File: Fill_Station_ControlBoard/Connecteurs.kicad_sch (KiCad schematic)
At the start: 45 parts, among them J3 USB_C_Receptacle_USB2.0_14P, J4 DE9_Pins, J6 RJ45_Wuerth_7499010211A, U2 USBLC6-2SC6, U3 MCP2561-E-P, U5 LAN8742A

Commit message: petites modifs pour ethernet + usb
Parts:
- added C35: 10n, symbol Device:C
- C11: value ~ -> 10n
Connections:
- net GND: now also C35.2; no longer J3.S1 (SHIELD)
- new net: C35.1, J3.S1 (SHIELD)
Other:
- note added: "Placer esd très proche du port"
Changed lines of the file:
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@@
 		)
 	)
+	(text "Placer esd très proche du port\n"
+		(exclude_from_sim no)
+		(at 316.484 36.322 0)
+		(effects
+			(font
+				(size 1.27 1.27)
+			)
+		)
+	)
 	(text "C'est normal que la pin VDDCR n'est pas alimenté - mettre les cap très proche de la chip\n"
 		(exclude_from_sim no)
@@
 	)
 	(junction
-		(at 294.64 101.6)
-		(diameter 0)
-		(color 0 0 0 0)
-	)
-	(junction
 		(at 88.9 189.23)
 		(diameter 0)
@@
 	)
 	(junction
+		(at 294.64 106.68)
+		(diameter 0)
+		(color 0 0 0 0)
+	)
+	(junction
 		(at 49.53 72.39)
 		(diameter 0)
@@
 	(wire
 		(pts
-			(xy 287.02 101.6) (xy 294.64 101.6)
-		)
-		(stroke
-			(width 0)
-			(type default)
-		)
-	)
-	(wire
-		(pts
 			(xy 152.4 64.77) (xy 119.38 64.77)
 		)
@@
 	(wire
 		(pts
-			(xy 294.64 99.06) (xy 294.64 101.6)
+			(xy 294.64 99.06) (xy 294.64 106.68)
+		)
+		(stroke
+			(width 0)
+			(type default)
+		)
+	)
+	(wire
+		(pts
+			(xy 294.64 106.68) (xy 294.64 109.22)
 		)
 		(stroke
@@
 	(wire
 		(pts
+			(xy 287.02 106.68) (xy 294.64 106.68)
+		)
+		(stroke
+			(width 0)
+			(type default)
+		)
+	)
+	(wire
+		(pts
 			(xy 93.98 199.39) (xy 93.98 217.17)
 		)
@@
 	(wire
 		(pts
-			(xy 294.64 101.6) (xy 294.64 104.14)
-		)
-		(stroke
-			(width 0)
-			(type default)
-		)
-	)
-	(wire
-		(pts
 			(xy 314.96 78.74) (xy 314.96 81.28)
 		)
@@
 		)
 	)
-	(wire
-		(pts
-			(xy 287.02 99.06) (xy 287.02 101.6)
-		)
-		(stroke
-			(width 0)
-			(type default)
-		)
-	)
 	(label "LED2"
 		(at 149.86 232.41 0)
@@
 	(symbol
 		(lib_id "power:GND")
-		(at 294.64 104.14 0)
+		(at 294.64 109.22 0)
 		(unit 1)
 		(exclude_from_sim no)
@@
 		(fields_autoplaced yes)
 		(property "Reference" "#PWR014"
-			(at 294.64 110.49 0)
+			(at 294.64 115.57 0)
 			(effects
 				(font
@@
 		)
 		(property "Value" "GND"
-			(at 294.64 109.22 0)
+			(at 294.64 114.3 0)
 			(effects
 				(font
@@
 		)
 		(property "Footprint" ""
-			(at 294.64 104.14 0)
+			(at 294.64 109.22 0)
 			(effects
 				(font
@@
 		)
 		(property "Datasheet" ""
-			(at 294.64 104.14 0)
+			(at 294.64 109.22 0)
 			(effects
 				(font
@@
 		)
 		(property "Description" "Power symbol creates a global label with name \"GND\" , ground"
-			(at 294.64 104.14 0)
+			(at 294.64 109.22 0)
 			(effects
 				(font
@@
 			)
 		)
-		(property "Value" "~"
+		(property "Value" "10n"
 			(at 240.03 231.1399 0)
 			(effects
@@
 					(unit 1)
 				)
+			)
+		)
+	)
+	(symbol
+		(lib_id "Device:C")
+		(at 287.02 102.87 0)
+		(unit 1)
+		(exclude_from_sim no)
+		(in_bom yes)
+		(on_board yes)
+		(dnp no)
+		(property "Reference" "C35"
+			(at 290.83 101.5999 0)
+			(effects
+				(font
+					(size 1.27 1.27)
+				)
+				(justify left)
+			)
+		)
+		(property "Value" "10n"
+			(at 290.83 104.1399 0)
+			(effects
+				(font
+					(size 1.27 1.27)
+				)
+				(justify left)
+			)
+		)
+		(property "Footprint" ""
+			(at 287.9852 106.68 0)
+			(effects
+				(font
+					(size 1.27 1.27)
+				)
+				(hide yes)
+			)
+		)
+		(property "Datasheet" "~"
+			(at 287.02 102.87 0)
+			(effects
+				(font
+					(size 1.27 1.27)
+				)
+				(hide yes)
+			)
+		)
+		(property "Description" "Unpolarized capacitor"
+			(at 287.02 102.87 0)
+			(effects
+				(font
+					(size 1.27 1.27)
+				)
+				(hide yes)
+			)
+		)
+		(pin "1"
+		)
+		(pin "2"
+		)
+		(instances
+			(project "Fill_Station_ControlBoard"
+				(path "/eaacffe0-ee57-428e-a37e-5655e0922ccc/08c8ede8-1095-4e69-9f52-7f615080da19"
+					(reference "C35")
+					(unit 1)
+				)

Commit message: heater
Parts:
- removed D4: D, symbol Device:D
- added R41: 100, symbol Device:R_US
- added U4: TCAN337G, symbol Interface_CAN_LIN:TCAN337G
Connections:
- net +3.3V is gone; now on net 3V3: R6.1
- net +5V: now also D3.1 (K), F3.2
- net TX_N: now reaches J6.2 (TD-), U5.20 (TXN)
- net TX_N: now also R41.2
- net TX_P: now reaches J6.1 (TD+), U5.21 (TXP)
- net TX_P: now also R41.1
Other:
- note added: "pull up?"

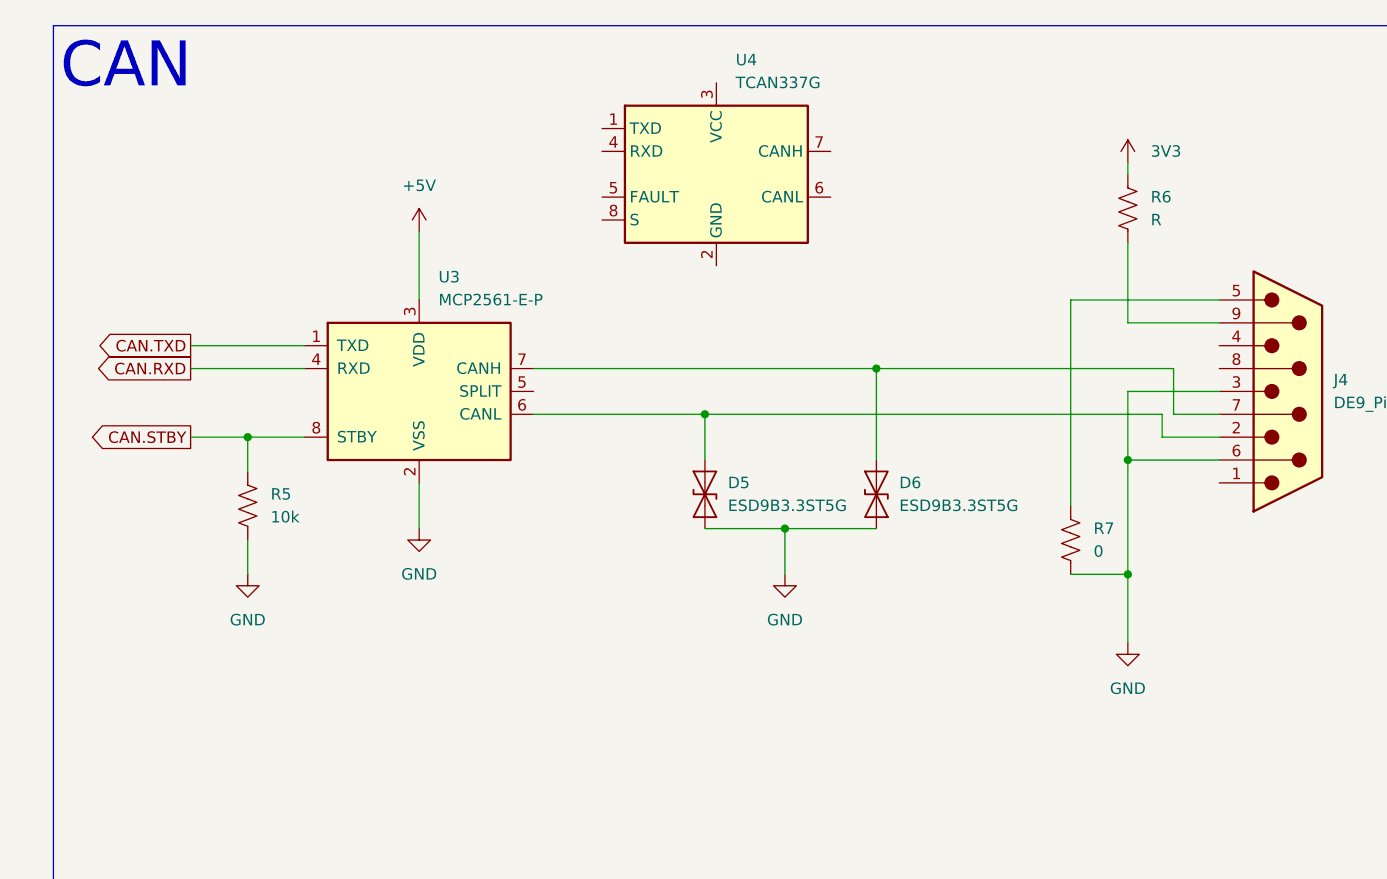
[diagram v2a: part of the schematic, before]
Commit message: Développer plus le circuit CAN
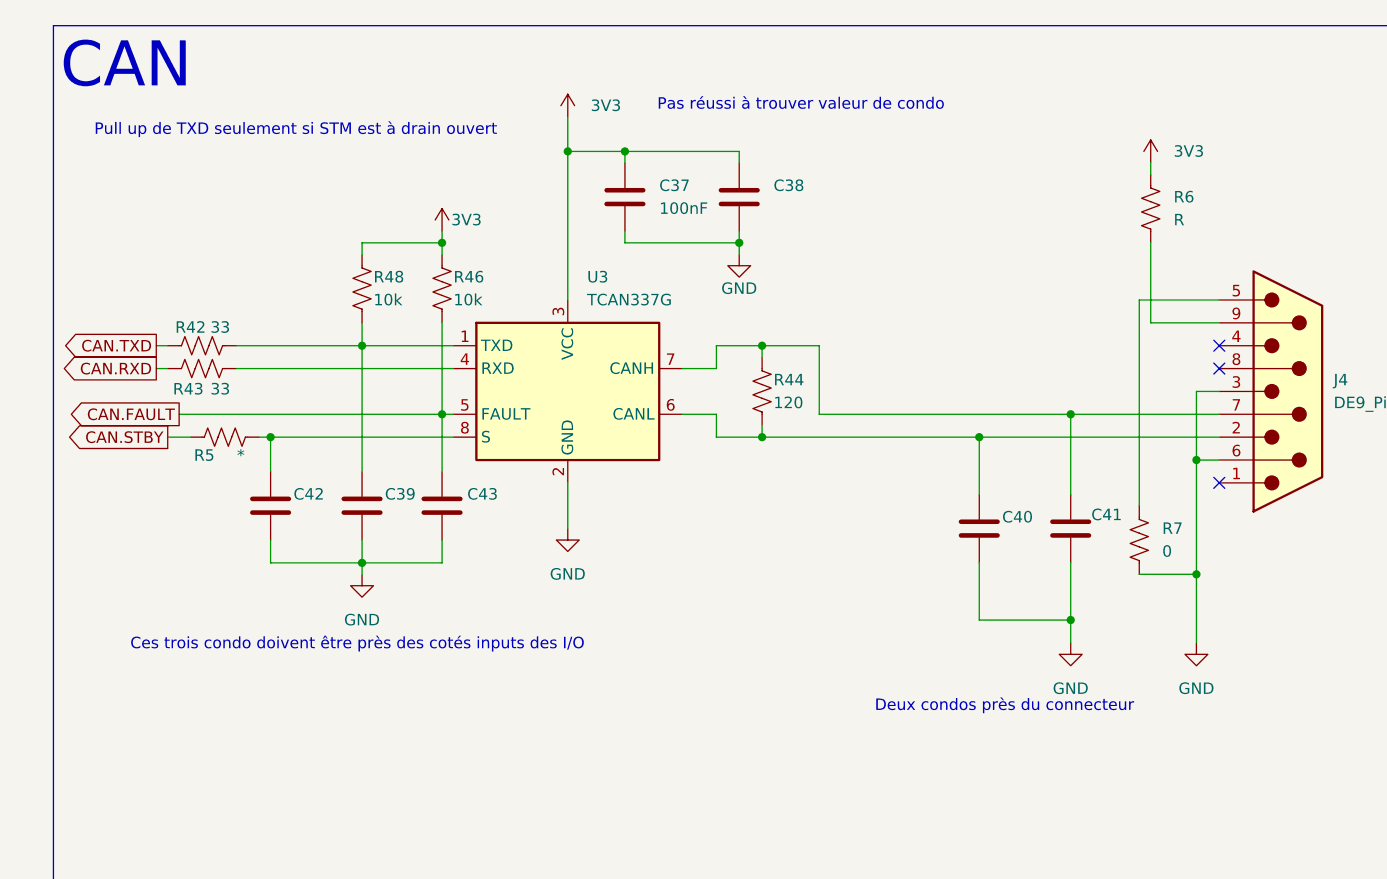
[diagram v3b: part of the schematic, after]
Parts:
- removed D5, D6: ESD9B3.3ST5G, Diode_SMD:D_SOD-923, symbol Diode:ESD9B3.3ST5G
- removed U3: MCP2561-E-P, Package_DIP:DIP-8_W7.62mm, symbol Interface_CAN_LIN:MCP2561-E-P
- removed U4: TCAN337G, symbol Interface_CAN_LIN:TCAN337G
- added C37: 100nF, symbol Device:C
- added C38, C39, C40, C41, C42, C43: ~, symbol Device:C
- added R42, R43: 33, symbol Device:R_US
- added R44: 120, symbol Device:R_US
- added R46, R48: 10k, symbol Device:R_US
- added U3: TCAN337G, symbol Interface_CAN_LIN:TCAN337G
- R5: value 10k -> *
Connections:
- net 3V3: now also C37.1, C38.1, R46.1, R48.1, U3.3 (VCC)
- net CAN.RXD: now also R43.1
- net CAN.TXD: now also R42.1
- net GND: now also C37.2, C38.2, C39.2, C40.2, C41.2, C42.2, C43.2, U3.2 (GND); no longer R5.2
- net at J4.2: now also C40.1, R44.2, U3.6 (CANL)
- net at J4.7: now also C41.1, R44.1, U3.7 (CANH)
- new net: C39.1, R42.2, R48.2, U3.1 (TXD)
- new net: R43.2, U3.4 (RXD)
- new net: C42.1, R5.2, U3.8 (S)
- new net CAN.FAULT: C43.1, R46.2, U3.5 (FAULT)
- no-connect marks 1 -> 4
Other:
- note added: "Ces trois condo doivent être près des cotés inputs des I/O"
- note added: "Deux condos près du connecteur"
- note added: "Pas réussi à trouver valeur de condo"
- note added: "Pull up de TXD seulement si STM est à drain ouvert"
- moved on the sheet: R6, R7

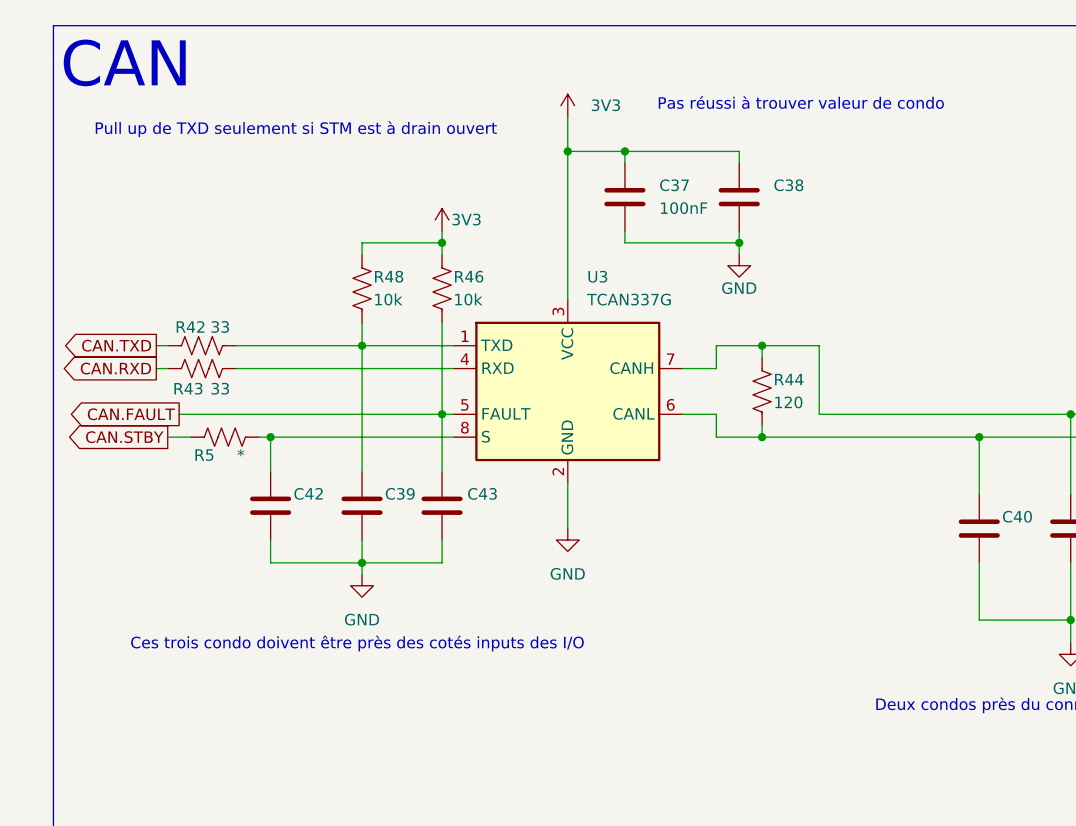
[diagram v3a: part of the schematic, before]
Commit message: Ajouter schema de JTAG
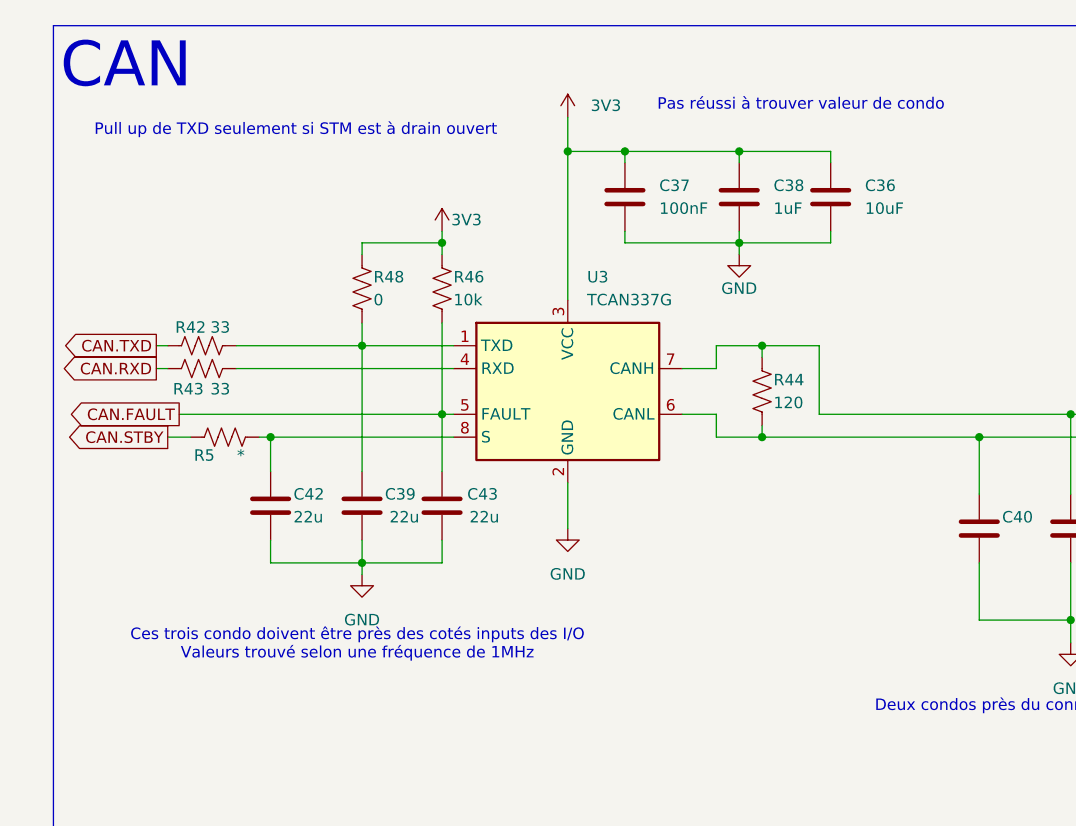
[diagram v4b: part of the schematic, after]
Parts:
- added C36: 10uF, symbol Device:C
- C38: value ~ -> 1uF
- C39, C42, C43: value ~ -> 22u
- R48: value 10k -> 0
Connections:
- net 3V3: now also C36.1
- net GND: now also C36.2
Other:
- note added: "Ces trois condo doivent être près des cotés inputs des I/O Valeurs trouvé selon une fréquence de 1MHz"
- note removed: "Ces trois condo doivent être près des cotés inputs des I/O"
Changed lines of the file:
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@@
 		)
 	)
-	(text "Ces trois condo doivent être près des cotés inputs des I/O\n"
+	(text "Ces trois condo doivent être près des cotés inputs des I/O \nValeurs trouvé selon une fréquence de 1MHz\n"
 		(exclude_from_sim no)
 		(at 61.722 95.504 0)
@@
 	)
 	(junction
+		(at 104.14 40.64)
+		(diameter 0)
+		(color 0 0 0 0)
+	)
+	(junction
 		(at 358.14 60.96)
 		(diameter 0)
@@
 	(wire
 		(pts
+			(xy 114.3 40.64) (xy 114.3 41.91)
+		)
+		(stroke
+			(width 0)
+			(type default)
+		)
+	)
+	(wire
+		(pts
 			(xy 62.23 62.23) (xy 62.23 76.2)
 		)
@@
 	(wire
 		(pts
+			(xy 104.14 50.8) (xy 114.3 50.8)
+		)
+		(stroke
+			(width 0)
+			(type default)
+		)
+	)
+	(wire
+		(pts
 			(xy 72.39 207.01) (xy 106.68 207.01)
 		)
@@
 	(wire
 		(pts
+			(xy 104.14 40.64) (xy 114.3 40.64)
+		)
+		(stroke
+			(width 0)
+			(type default)
+		)
+	)
+	(wire
+		(pts
 			(xy 104.14 49.53) (xy 104.14 50.8)
 		)
@@
 	(wire
 		(pts
+			(xy 114.3 49.53) (xy 114.3 50.8)
+		)
+		(stroke
+			(width 0)
+			(type default)
+		)
+	)
+	(wire
+		(pts
 			(xy 231.14 224.79) (xy 231.14 227.33)
 		)
@@
 			)
 		)
-		(property "Value" "10k"
+		(property "Value" "0"
 			(at 63.5 57.15 0)
 			(effects
@@
 			)
 		)
-		(property "Value" "~"
+		(property "Value" "22u"
 			(at 65.278 81.28 0)
 			(effects
@@
 			)
 		)
-		(property "Value" "~"
+		(property "Value" "22u"
 			(at 54.61 81.2799 0)
 			(effects
@@
 			)
 		)
-		(property "Value" "~"
+		(property "Value" "1uF"
 			(at 107.95 46.9899 0)
 			(effects
@@
 			)
 		)
-		(property "Value" "~"
+		(property "Value" "22u"
 			(at 74.168 81.28 0)
 			(effects
@@
 					(unit 1)
 				)
+			)
+		)
+	)
+	(symbol
+		(lib_id "Device:C")
+		(at 114.3 45.72 0)
+		(unit 1)
+		(exclude_from_sim no)
+		(in_bom yes)
+		(on_board yes)
+		(dnp no)
+		(fields_autoplaced yes)
+		(property "Reference" "C36"
+			(at 118.11 44.4499 0)
+			(effects
+				(font
+					(size 1.27 1.27)
+				)
+				(justify left)
+			)
+		)
+		(property "Value" "10uF"
+			(at 118.11 46.9899 0)
+			(effects
+				(font
+					(size 1.27 1.27)
+				)
+				(justify left)
+			)
+		)
+		(property "Footprint" ""
+			(at 115.2652 49.53 0)
+			(effects
+				(font
+					(size 1.27 1.27)
+				)
+				(hide yes)
+			)
+		)
+		(property "Datasheet" "~"
+			(at 114.3 45.72 0)
+			(effects
+				(font
+					(size 1.27 1.27)
+				)
+				(hide yes)
+			)
+		)
+		(property "Description" "Unpolarized capacitor"
+			(at 114.3 45.72 0)
+			(effects
+				(font
+					(size 1.27 1.27)
+				)
+				(hide yes)
+			)
+		)
+		(pin "1"
+		)
+		(pin "2"
+		)
+		(instances
+			(project "Fill_Station_ControlBoard"
+				(path "/eaacffe0-ee57-428e-a37e-5655e0922ccc/08c8ede8-1095-4e69-9f52-7f615080da19"
+					(reference "C36")
+					(unit 1)
+				)
